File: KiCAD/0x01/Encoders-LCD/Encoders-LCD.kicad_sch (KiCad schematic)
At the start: 29 parts, among them J1 I2C_Conn, J2 Conn_01x05, SW1 SW_SHIFT, SW2 SW_LEFT, SW3 SW_RIGHT, U4 A_REG, U5 B_REG, U6 SW_REG

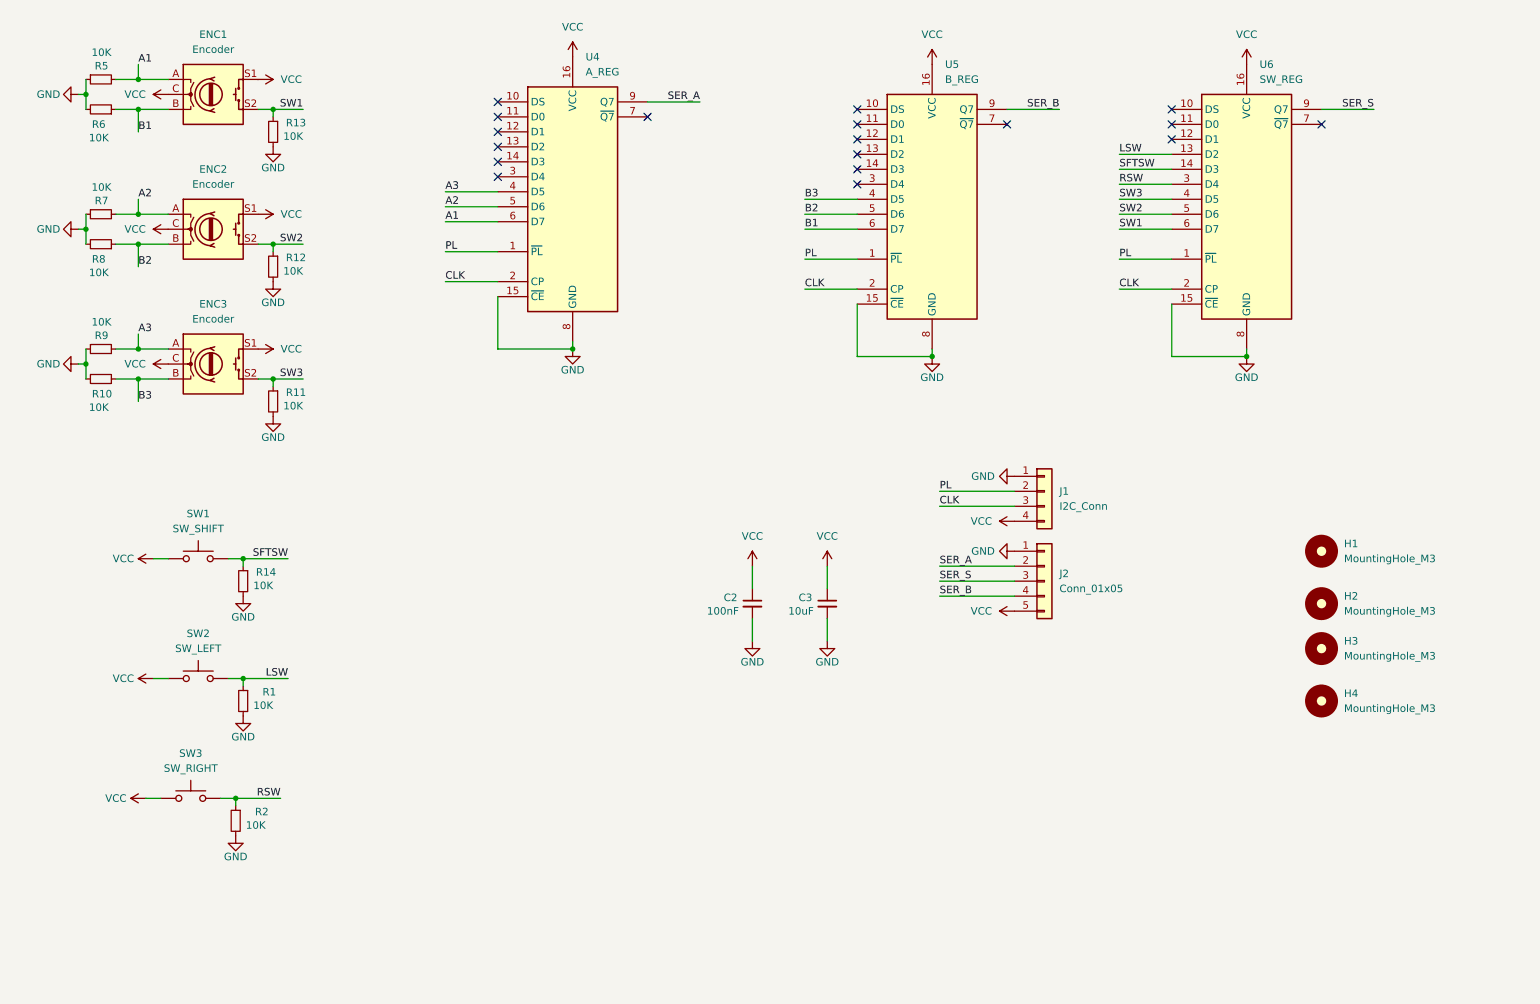
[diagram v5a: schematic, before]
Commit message: encoders lcd finished
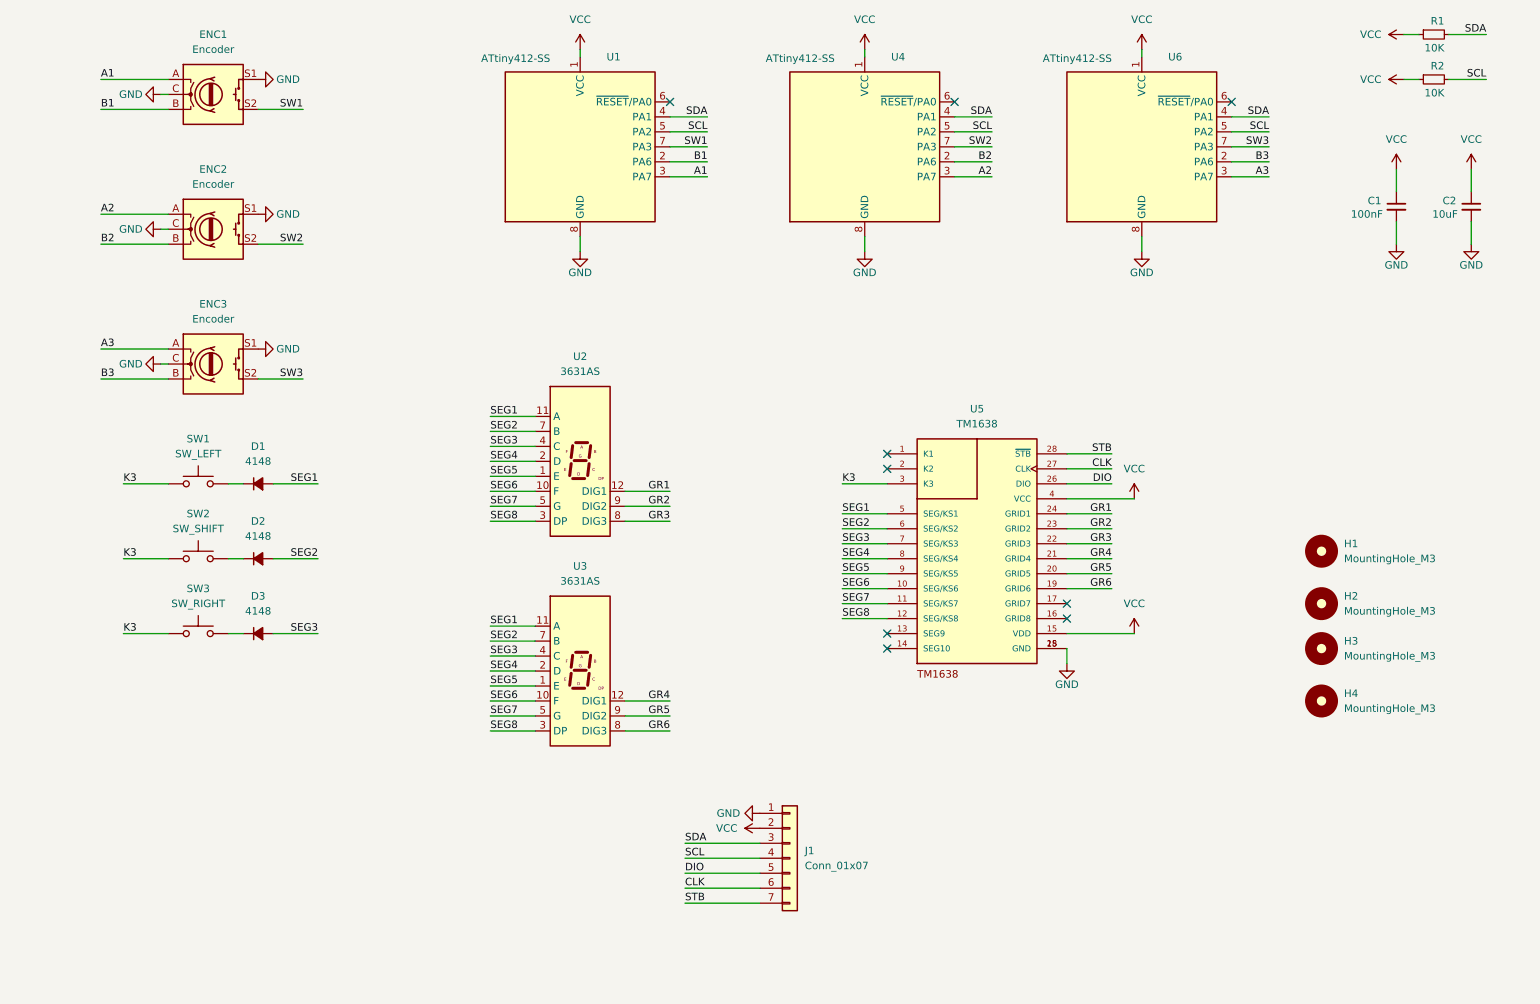
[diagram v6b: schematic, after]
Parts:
- removed J1: I2C_Conn, Connector_PinHeader_2.54mm:PinHeader_1x04_P2.54mm_Vertical, symbol Connector_Generic:Conn_01x04
- removed J2: Conn_01x05, Connector_PinHeader_2.54mm:PinHeader_1x05_P2.54mm_Vertical, symbol Connector_Generic:Conn_01x05
- removed R10, R11, R12, R13, R14, R5, R6, R7, R8, R9: 10K, Capacitor_SMD:C_0805_2012Metric_Pad1.18x1.45mm_HandSolder, symbol Device:R_Small
- removed U4: A_REG, Package_SO:SOIC-16_3.9x9.9mm_P1.27mm, symbol 74xx:74HC165
- removed U5: B_REG, Package_SO:SOIC-16_3.9x9.9mm_P1.27mm, symbol 74xx:74HC165
- removed U6: SW_REG, Package_SO:SOIC-16_3.9x9.9mm_P1.27mm, symbol 74xx:74HC165
- added D1, D2, D3: 4148, PCM_Diode_SMD_Handsoldering_AKL:D_SOD-123, symbol Device:D_Small_Filled
- added J1: Conn_01x07, Connector_JST:JST_PH_S7B-PH-K_1x07_P2.00mm_Horizontal, symbol Connector_Generic:Conn_01x07
- added U1, U4, U6: ATtiny412-SS, Package_SO:SOIC-8_3.9x4.9mm_P1.27mm, symbol MCU_Microchip_ATtiny:ATtiny412-SS
- added U2, U3: 3631AS, shared:3631AS, symbol 0x01-Library:3631AS
- added U5: TM1638, shared:SOIC127P1041X265-28N, symbol TM1638:TM1638
- renumbered C2 to C1, C3 to C2, SW2 to SW1, SW1 to SW2
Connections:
- net A1: now also U1.3 (PA7)
- net A2: now also U4.3 (PA7)
- net A3: now also U6.3 (PA7)
- net B1: now also U1.2 (PA6)
- net B2: now also U4.2 (PA6)
- net B3: now also U6.2 (PA6)
- net CLK: now also J1.6 (Pin_6), U5.27 (CLK)
- net GND: now also ENC1.C, ENC1.S1, ENC2.C, ENC2.S1, ENC3.C, ENC3.S1, J1.1 (Pin_1), U1.8 (GND), U4.8 (GND), U5.18 (GND), U5.25 (GND), U6.8 (GND); no longer R1.2, R2.2
- net SW1: now also U1.7 (PA3)
- net SW2: now also U4.7 (PA3)
- net SW3: now also U6.7 (PA3)
- net VCC: now also R1.1, R2.1, J1.2 (Pin_2), U1.1 (VCC), U4.1 (VCC), U5.15 (VDD), U5.4 (VCC), U6.1 (VCC); no longer ENC1.C, ENC1.S1, ENC2.C, ENC2.S1, ENC3.C, ENC3.S1, SW1.1, SW2.1, SW3.1
- net LSW: no longer names the net of SW1.2
- net LSW: now also D1.1 (K); no longer R1.1
- net RSW: no longer names the net of SW3.2
- net RSW: now also D3.1 (K); no longer R2.1
- net SFTSW: no longer names the net of SW2.2
- net SFTSW: now also D2.1 (K)
- new net DIO: J1.5 (Pin_5), U5.26 (DIO)
- new net GR1: U2.12 (DIG1), U5.24 (GRID1)
- new net GR2: U2.9 (DIG2), U5.23 (GRID2)
- new net GR3: U2.8 (DIG3), U5.22 (GRID3)
- new net GR4: U3.12 (DIG1), U5.21 (GRID4)
- new net GR5: U3.9 (DIG2), U5.20 (GRID5)
- new net GR6: U3.8 (DIG3), U5.19 (GRID6)
- new net K3: SW1.1, SW2.1, SW3.1, U5.3 (K3)
- new net SCL: J1.4 (Pin_4), R2.2, U1.5 (PA2), U4.5 (PA2), U6.5 (PA2)
- new net SDA: J1.3 (Pin_3), R1.2, U1.4 (PA1), U4.4 (PA1), U6.4 (PA1)
- new net SEG1: D1.2 (A), U2.11 (A), U3.11 (A), U5.5 (SEG/KS1)
- new net SEG2: D2.2 (A), U2.7 (B), U3.7 (B), U5.6 (SEG/KS2)
- new net SEG3: D3.2 (A), U2.4 (C), U3.4 (C), U5.7 (SEG/KS3)
- new net SEG4: U2.2 (D), U3.2 (D), U5.8 (SEG/KS4)
- new net SEG5: U2.1 (E), U3.1 (E), U5.9 (SEG/KS5)
- new net SEG6: U2.10 (F), U3.10 (F), U5.10 (SEG/KS6)
- new net SEG7: U2.5 (G), U3.5 (G), U5.11 (SEG/KS7)
- new net SEG8: U2.3 (DP), U3.3 (DP), U5.12 (SEG/KS8)
- new net STB: J1.7 (Pin_7), U5.28 (~{STB})
- no-connect marks 18 -> 9
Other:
- moved on the sheet: C1, C2, SW1, SW3

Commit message: lcd encoders with ht16k33
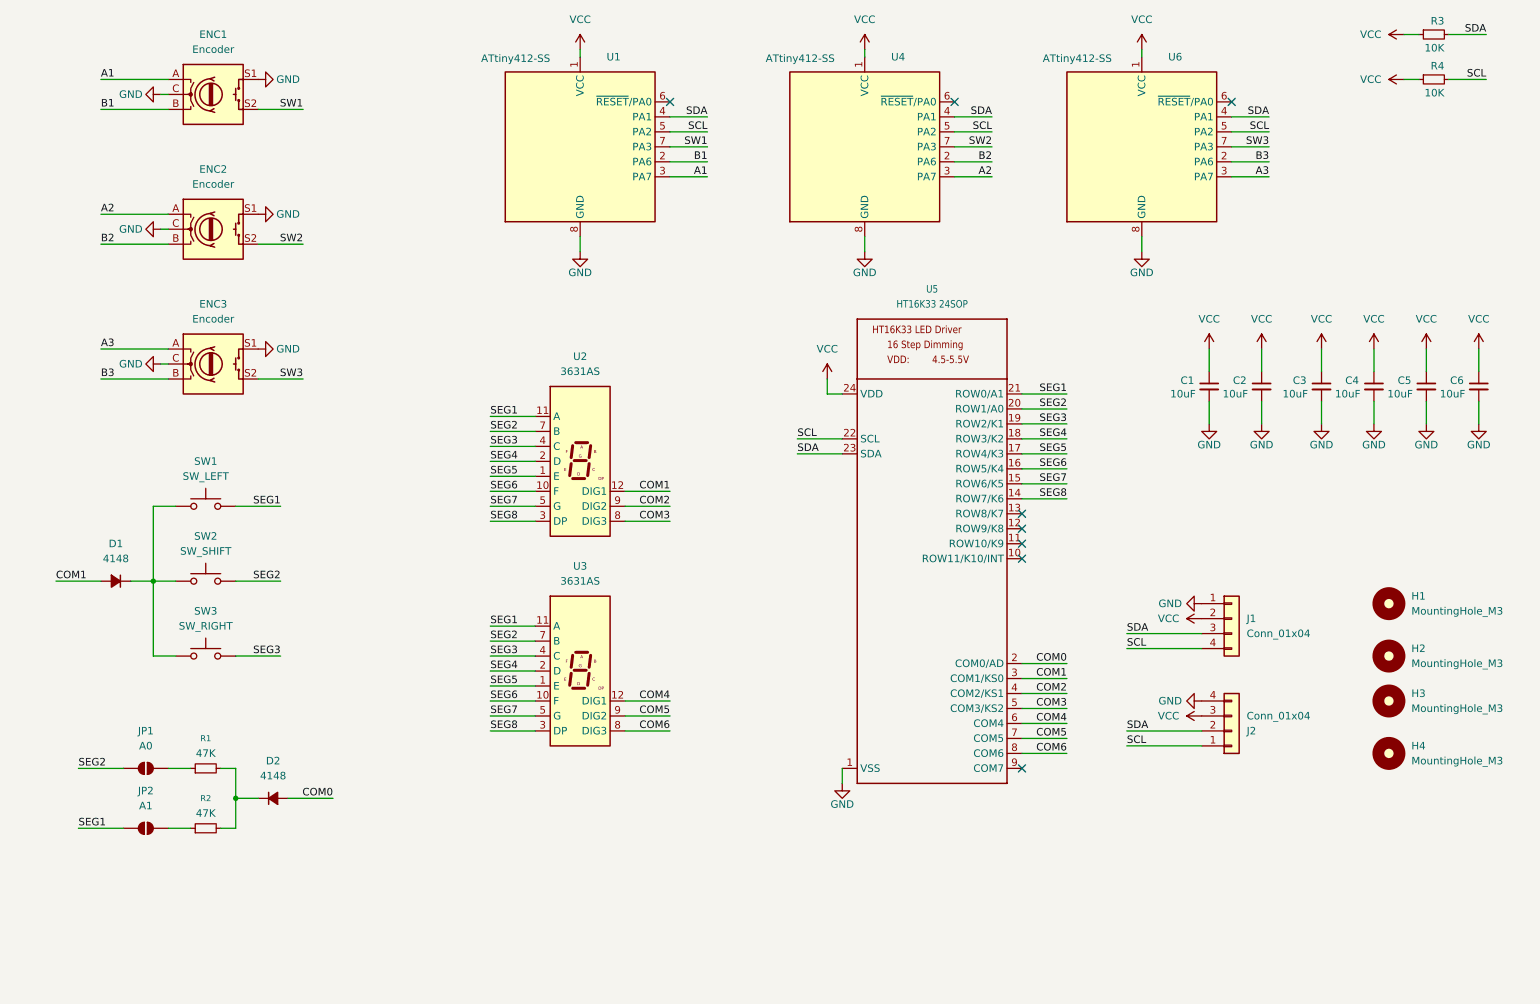
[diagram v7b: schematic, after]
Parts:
- removed C1: 100nF, Capacitor_SMD:C_0805_2012Metric_Pad1.18x1.45mm_HandSolder, symbol Device:C_Small
- removed D3: 4148, PCM_Diode_SMD_Handsoldering_AKL:D_SOD-123, symbol Device:D_Small_Filled
- removed J1: Conn_01x07, Connector_JST:JST_PH_S7B-PH-K_1x07_P2.00mm_Horizontal, symbol Connector_Generic:Conn_01x07
- removed U5: TM1638, shared:SOIC127P1041X265-28N, symbol TM1638:TM1638
- added C2, C3, C4, C5, C6: 10uF, Capacitor_SMD:C_0805_2012Metric_Pad1.18x1.45mm_HandSolder, symbol Device:C_Small
- added J1, J2: Conn_01x04, Connector_JST:JST_PH_S4B-PH-K_1x04_P2.00mm_Horizontal, symbol Connector_Generic:Conn_01x04
- added JP1: A0, Jumper:SolderJumper-2_P1.3mm_Open_RoundedPad1.0x1.5mm, symbol Jumper:SolderJumper_2_Open
- added JP2: A1, Jumper:SolderJumper-2_P1.3mm_Open_RoundedPad1.0x1.5mm, symbol Jumper:SolderJumper_2_Open
- added R1, R2: 47K, Resistor_SMD:R_0805_2012Metric_Pad1.20x1.40mm_HandSolder, symbol Device:R_Small
- added U5: HT16K33 24SOP, Package_SO:SSOP-24_5.3x8.2mm_P0.65mm, symbol ht16k33_sop28:HT16K33_SOP24
- renumbered C2 to C1, R1 to R3, R2 to R4
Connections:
- net K3 is gone; now on an unnamed net: SW1.1, SW2.1, SW3.1
- net GND: now also C2.2, C3.2, C4.2, C5.2, C6.2, J1.1 (Pin_1), J2.4 (Pin_4), U5.1 (VSS)
- net SCL: now also J1.4 (Pin_4), J2.1 (Pin_1), U5.22 (SCL)
- net SDA: now also J1.3 (Pin_3), J2.2 (Pin_2), U5.23 (SDA)
- net SEG1: now also SW1.2, JP2.1 (A), U5.21 (ROW0/A1); no longer D1.2 (A)
- net SEG2: now also SW2.2, JP1.1 (A), U5.20 (ROW1/A0); no longer D2.2 (A)
- net SEG3: now also SW3.2, U5.19 (ROW2/K1)
- net SEG4: now also U5.18 (ROW3/K2)
- net SEG5: now also U5.17 (ROW4/K3)
- net SEG6: now also U5.16 (ROW5/K4)
- net SEG7: now also U5.15 (ROW6/K5)
- net SEG8: now also U5.14 (ROW7/K6)
- net VCC: now also C2.1, C3.1, C4.1, C5.1, C6.1, J1.2 (Pin_2), J2.3 (Pin_3), U5.24 (VDD)
- net at D2.1 (K): now also R1.2, R2.2; no longer SW2.2
- net at D1.1 (K): no longer SW1.2
- net GR1 renamed COM1
- net COM1: now also D1.2 (A), U5.3 (COM1/KS0)
- net GR2 renamed COM2
- net COM2: now also U5.4 (COM2/KS1)
- net GR3 renamed COM3
- net COM3: now also U5.5 (COM3/KS2)
- net GR4 renamed COM4
- net COM4: now also U5.6 (COM4)
- net GR5 renamed COM5
- net COM5: now also U5.7 (COM5)
- net GR6 renamed COM6
- net COM6: now also U5.8 (COM6)
- new net: JP2.2 (B), R2.1
- new net: JP1.2 (B), R1.1
- new net COM0: D2.2 (A), U5.2 (COM0/AD)
- no-connect marks 9 -> 8
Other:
- moved on the sheet: C1, D1, H1, H2, H3, H4, SW1, SW2, SW3

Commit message: fixes
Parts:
- U5: footprint Package_SO:SSOP-24_5.3x8.2mm_P0.65mm -> Package_SO:SOP-24_7.5x15.4mm_P1.27mm
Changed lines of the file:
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@@
 			)
 		)
-		(property "Footprint" "Package_SO:SSOP-24_5.3x8.2mm_P0.65mm"
+		(property "Footprint" "Package_SO:SOP-24_7.5x15.4mm_P1.27mm"
 			(at 176.53 65.532 0)
 			(effects
